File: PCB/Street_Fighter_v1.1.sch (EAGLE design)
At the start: 49 parts, among them Q1 BSS138, Q2 BSS138, Q3 FQP30N06L, Q4 BSS138, Q5 BSS138, U1 ARDUINO_YUN_SHIELDYUN, U2 MCP6231RT-E/OT

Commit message: V5 Update
Added 3D printed parts

V5 - Trialling new Sonar detection algorithm
- Sonar must have 2 consecutive detections to register

PIR timeout changed from 5s to 2s.
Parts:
- removed JP1: ICSP Header, SparkFun-Connectors:M03X22X3_SILK_SM
- removed OF: ADNS3080, SparkFun-Connectors:M06SIP
- removed Q5: BSS138, SparkFun-DiscreteSemi:MOSFET-NCHANNELBSS123LT1G
- removed R14: PHOTOCELLPTH, SparkFun-Sensors:PHOTOCELLPTH
- removed R15: 10K, SparkFun-Passives:RESISTOR1206
- removed SJ1, SJ2: JUMPER-PAD-2-NC_BY_TRACE, SparkFun-Passives:JUMPER-PAD-2-NC_BY_TRACE
- RTC: device SparkFun-Connectors:M04PTH -> SparkFun-Connectors:M05PTH
- TEMP: device SparkFun-Sensors:TMP36GT9 -> SparkFun-Connectors:M03PTH
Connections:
- removed net FLOW-SS: OF.2, U1.D12*
- removed net LIGHT-STATUS: R14.P$2, R15.1, U1.A0
- removed net MISO: JP1.1, OF.3
- removed net MLX-PWM: U1.D11*
- removed net MOSI: JP1.4, OF.4
- removed net SCK: JP1.3, OF.5
- new net SQW: RTC.3
- net +5V: now also RTC.5, TEMP.3; no longer JP1.2, OF.6, R15.2, RTC.4, TEMP.VCC
- net GND: now also RTC.4, TEMP.1; no longer JP1.6, OF.1, Q5.S, R14.P$1, RTC.1, TEMP.GND
- net LED-CONTROL: no longer Q5.G
- net LED-CONTROL-OUT: no longer Q5.D
- net SCL: no longer LIDAR.2, SJ2.1, SJ2.2
- net SDA: now also RTC.1; no longer LIDAR.3, RTC.3, SJ1.1, SJ1.2
- net TEMP: now also TEMP.2; no longer TEMP.VOUT
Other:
- note removed: "Lamp Status"
- note removed: "Optical Flow"
- moved on the sheet: C2, C7, HUMD, Q3, R16, T-ROAD, TEMP

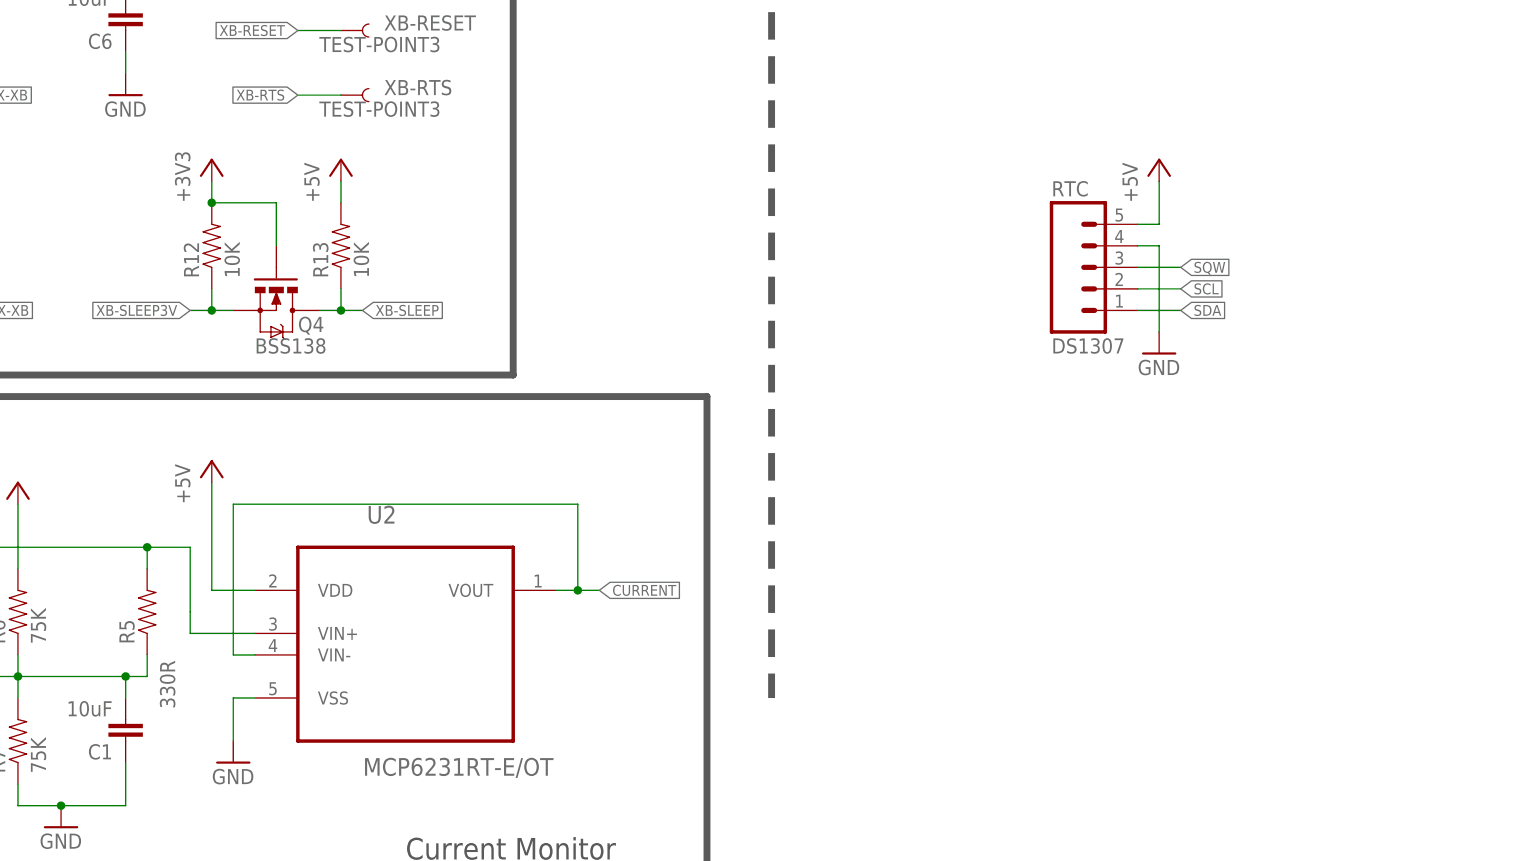
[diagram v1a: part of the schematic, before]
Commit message: Removed XBEE API code; now using transparent mode
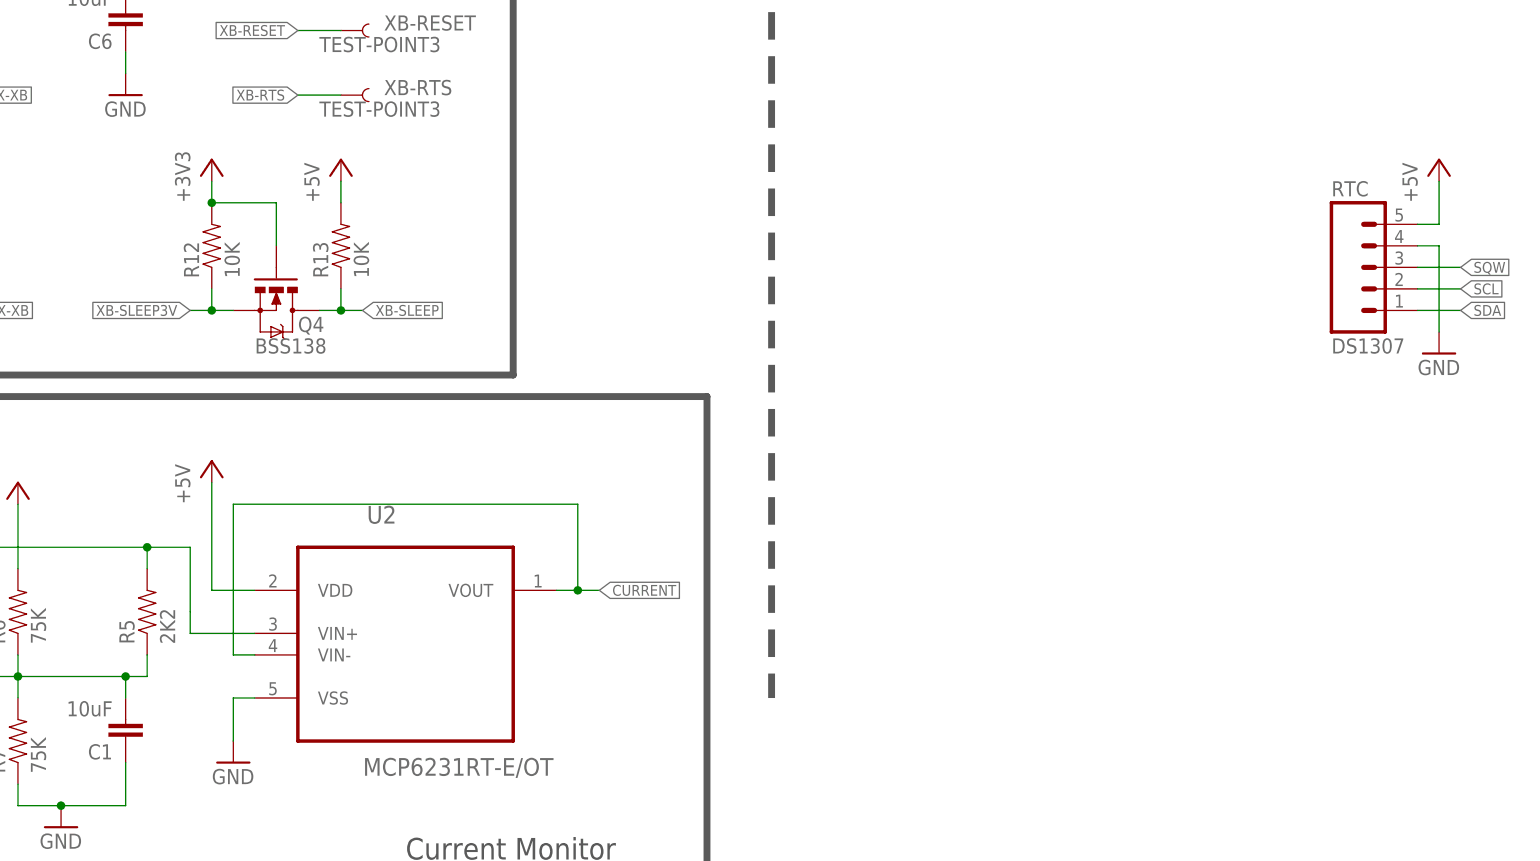
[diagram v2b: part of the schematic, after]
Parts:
- R5: value 330R -> 2K2
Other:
- moved on the sheet: RTC
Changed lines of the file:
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@@
 <?xml version="1.0" encoding="utf-8"?>
 <!DOCTYPE eagle SYSTEM "eagle.dtd">
-<eagle version="7.2.0">
+<eagle version="7.5.0">
 <drawing>
 <settings>
@@
 <setting verticaltext="up"/>
 </settings>
-<grid distance="0.1" unitdist="inch" unit="inch" style="lines" multiple="1" display="yes" altdistance="0.01" altunitdist="inch" altunit="inch"/>
+<grid distance="0.1" unitdist="inch" unit="inch" style="lines" multiple="1" display="no" altdistance="0.01" altunitdist="inch" altunit="inch"/>
 <layers>
 <layer number="1" name="Top" color="4" fill="1" visible="no" active="no"/>
@@
 <part name="P+8" library="supply1" deviceset="+5V" device=""/>
 <part name="GND6" library="supply1" deviceset="GND" device=""/>
-<part name="R5" library="SparkFun-Passives" deviceset="RESISTOR" device="1206" value="330R"/>
+<part name="R5" library="SparkFun-Passives" deviceset="RESISTOR" device="1206" value="2K2 "/>
 <part name="R6" library="SparkFun-Passives" deviceset="RESISTOR" device="1206" value="75K"/>
 <part name="R7" library="SparkFun-Passives" deviceset="RESISTOR" device="1206" value="75K"/>
@@
 <instance part="R5" gate="G$1" x="218.44" y="35.56" smashed="yes" rot="R90">
 <attribute name="NAME" x="216.9414" y="31.75" size="1.778" layer="95" rot="R90"/>
-<attribute name="VALUE" x="221.742" y="24.13" size="1.778" layer="96" rot="R90"/>
+<attribute name="VALUE" x="221.742" y="31.75" size="1.778" layer="96" rot="R90"/>
 </instance>
 <instance part="R6" gate="G$1" x="203.2" y="35.56" rot="R90"/>
@@
 <instance part="C2" gate="G$1" x="160.02" y="154.94" rot="R180"/>
 <instance part="TEMP" gate="G$1" x="66.04" y="149.86"/>
-<instance part="RTC" gate="G$1" x="327.66" y="76.2"/>
-<instance part="P+17" gate="1" x="337.82" y="88.9"/>
-<instance part="GND15" gate="1" x="337.82" y="66.04"/>
+<instance part="RTC" gate="G$1" x="360.68" y="76.2"/>
+<instance part="P+17" gate="1" x="370.84" y="88.9"/>
+<instance part="GND15" gate="1" x="370.84" y="66.04"/>
 </instances>
 <busses>
@@
 <segment>
 <pinref part="RTC" gate="G$1" pin="1"/>
-<wire x1="335.28" y1="71.12" x2="340.36" y2="71.12" width="0.2032" layer="91"/>
-<label x="340.36" y="71.12" size="1.27" layer="95" xref="yes"/>
+<wire x1="368.3" y1="71.12" x2="373.38" y2="71.12" width="0.2032" layer="91"/>
+<label x="373.38" y="71.12" size="1.27" layer="95" xref="yes"/>
 </segment>
 </net>
@@
 <segment>
 <pinref part="RTC" gate="G$1" pin="2"/>
-<wire x1="335.28" y1="73.66" x2="340.36" y2="73.66" width="0.2032" layer="91"/>
-<label x="340.36" y="73.66" size="1.27" layer="95" xref="yes"/>
+<wire x1="368.3" y1="73.66" x2="373.38" y2="73.66" width="0.2032" layer="91"/>
+<label x="373.38" y="73.66" size="1.27" layer="95" xref="yes"/>
 </segment>
 </net>
@@
 <segment>
 <pinref part="RTC" gate="G$1" pin="5"/>
-<wire x1="335.28" y1="81.28" x2="337.82" y2="81.28" width="0.2032" layer="91"/>
+<wire x1="368.3" y1="81.28" x2="370.84" y2="81.28" width="0.2032" layer="91"/>
 <pinref part="P+17" gate="1" pin="+5V"/>
-<wire x1="337.82" y1="81.28" x2="337.82" y2="86.36" width="0.2032" layer="91"/>
+<wire x1="370.84" y1="81.28" x2="370.84" y2="86.36" width="0.2032" layer="91"/>
 </segment>
 </net>
@@
 <segment>
 <pinref part="RTC" gate="G$1" pin="4"/>
-<wire x1="335.28" y1="78.74" x2="337.82" y2="78.74" width="0.2032" layer="91"/>
-<wire x1="337.82" y1="78.74" x2="337.82" y2="68.58" width="0.2032" layer="91"/>
+<wire x1="368.3" y1="78.74" x2="370.84" y2="78.74" width="0.2032" layer="91"/>
+<wire x1="370.84" y1="78.74" x2="370.84" y2="68.58" width="0.2032" layer="91"/>
 <pinref part="GND15" gate="1" pin="GND"/>
 </segment>
@@
 <segment>
 <pinref part="RTC" gate="G$1" pin="3"/>
-<wire x1="335.28" y1="76.2" x2="340.36" y2="76.2" width="0.2032" layer="91"/>
-<label x="340.36" y="76.2" size="1.27" layer="95" xref="yes"/>
-</segment>
-</net>
+<wire x1="368.3" y1="76.2" x2="373.38" y2="76.2" width="0.2032" layer="91"/>
+<label x="373.38" y="76.2" size="1.27" layer="95" xref="yes"/>
+</segment>
+</net>
